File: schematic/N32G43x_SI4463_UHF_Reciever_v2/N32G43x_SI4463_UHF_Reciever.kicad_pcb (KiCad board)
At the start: 4 copper layers, 70.4 x 58.2 mm, 152 parts, among them J1 U.FL, J2 Conn_01x04_Socket, J3 USB_C_Receptacle_USB2.0_16P, J5 Conn_01x03_Socket, Q1 BC847BS, Q10 MMBT3904, Q11 MMBT3904, Q2 MMBT3904, Q3 BC847BS, Q4 BC847BS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

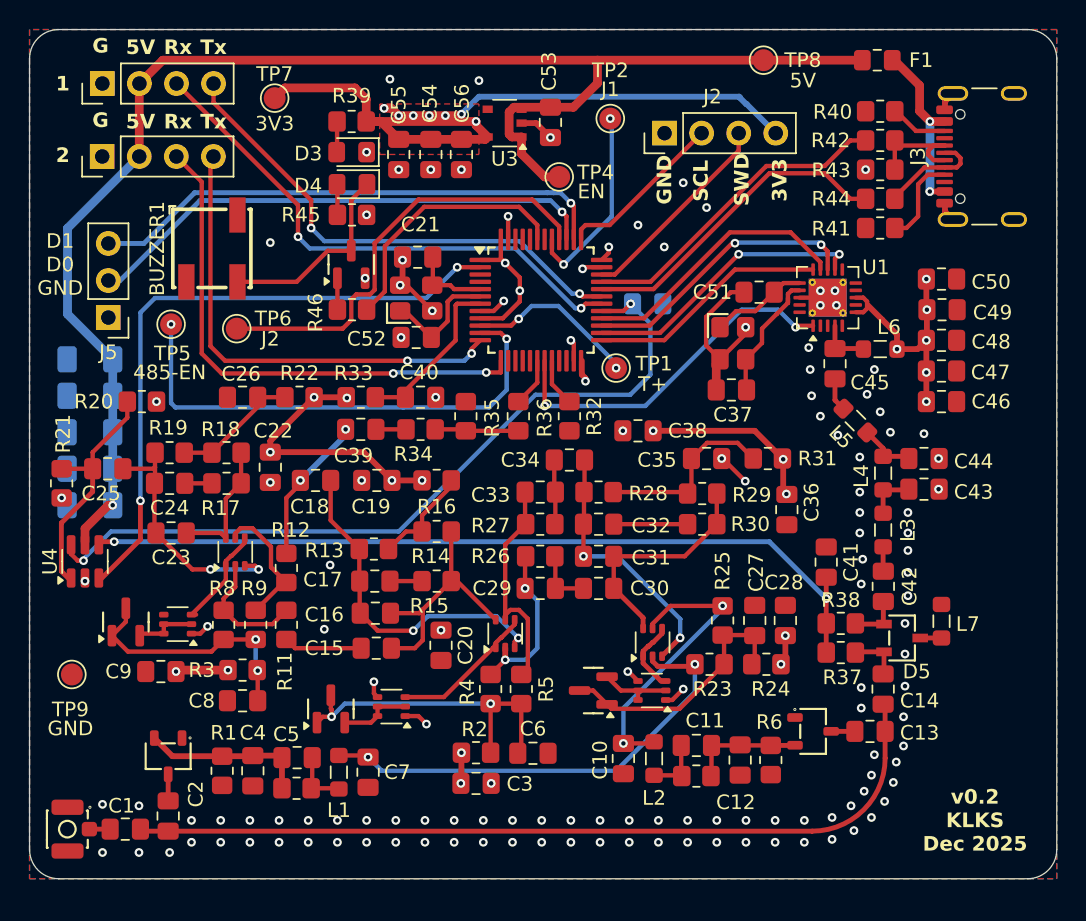
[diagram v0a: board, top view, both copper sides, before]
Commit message: Minor update to match pcb
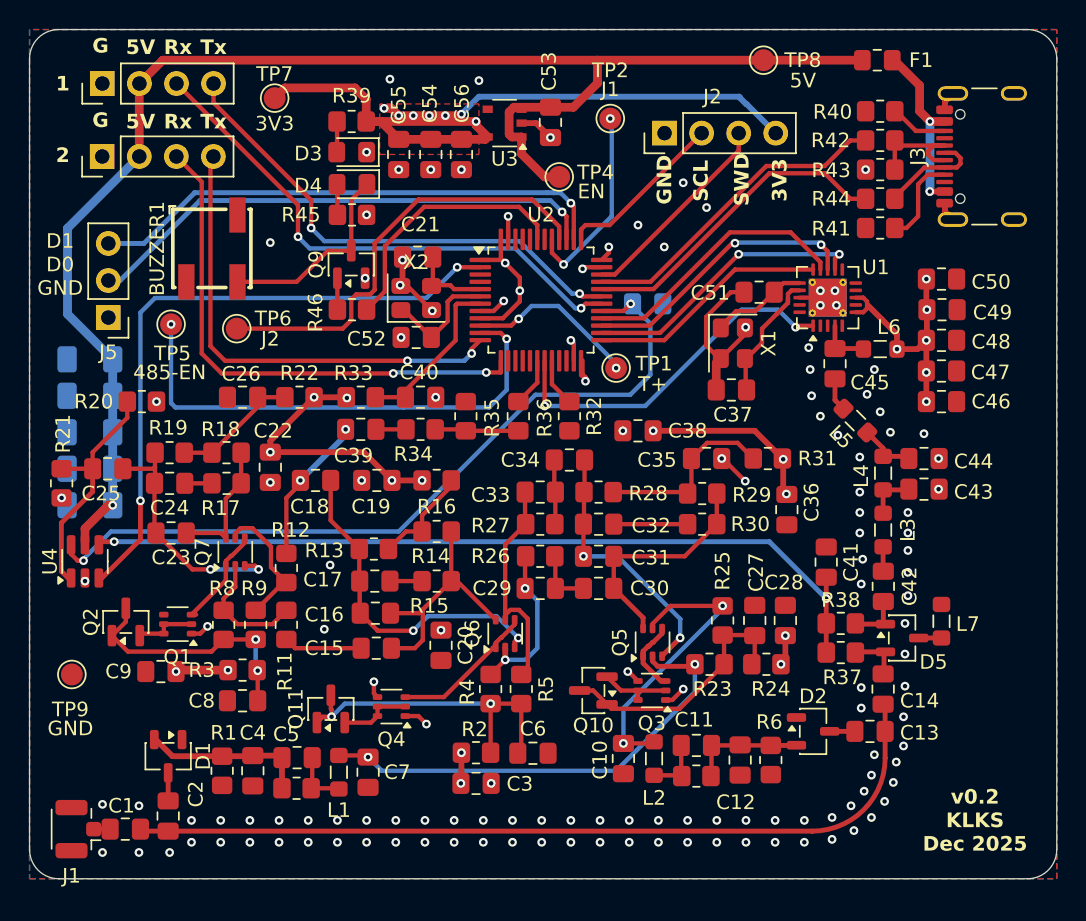
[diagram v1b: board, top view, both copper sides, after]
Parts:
- D1, D2: footprint PCM_JLCPCB:SOT-23-3_L2.9-W1.6-P1.90-LS2.8-BR -> Package_TO_SOT_SMD:SOT-23-3
- D5: footprint EasyEDA:SOT-23-3_L2.9-W1.6-P1.90-LS2.8-BR -> Package_TO_SOT_SMD:SOT-23-3
- J1: footprint PCM_JLCPCB:IPEX-SMD_BWIPX-1-001E -> Connector_Coaxial:U.FL_Hirose_U.FL-R-SMT-1_Vertical
- Q1, Q3, Q4, Q5, Q6, Q7: footprint PCM_JLCPCB:SOT-363_SC-70-6 -> Package_TO_SOT_SMD:SOT-363_SC-70-6
- Q10, Q11, Q2, Q9: footprint PCM_JLCPCB:Q_SOT-23 -> Package_TO_SOT_SMD:SOT-23
- U2: footprint PCM_JLCPCB:LQFP-48_7x7mm_P0.5mm -> Package_QFP:LQFP-48_7x7mm_P0.5mm
- X1, X2: footprint PCM_JLCPCB:OSC-SMD_4P-L3.2-W2.5-BL -> Oscillator:Oscillator_SMD_Abracon_ASE-4Pin_3.2x2.5mm
- turned C51 to 180 degrees
- turned D1 to -90 degrees
- turned D2 to 0 degrees
- turned D5 to 0 degrees
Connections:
- net VIA_P3 renamed /RF Circuit/VIA_P3
- net VIA_P4 renamed /RF Circuit/VIA_P4
- C12 pad 2: Net-(C11-Pad2) -> Net-(C11-Pad1)
- C51 pad 1: GND -> RF_X2
- C51 pad 2: RF_X2 -> GND
- C52 pad 1: GND -> MCU_X2
- C52 pad 2: MCU_X2 -> GND
- D2 pad 2: Net-(C11-Pad2) -> Net-(C11-Pad1)
- L2 pad 2: Net-(C11-Pad1) -> Net-(C11-Pad2)
- R3 pad 1: Net-(Q2-B) -> VDD_MCU
- R3 pad 2: VDD_MCU -> Net-(Q2-B)
- R36 pad 1: PC13 -> PB0
- R6 pad 1: Net-(C11-Pad2) -> Net-(C11-Pad1)
- R9 pad 1: Net-(Q2-B) -> Net-(Q7B-B2)
- R9 pad 2: Net-(Q7B-B2) -> Net-(Q2-B)
- U4 pad 3: PB0 -> PC13
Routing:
- net MCU_X2: vias 0 -> 1
- net GND: vias 132 -> 131
